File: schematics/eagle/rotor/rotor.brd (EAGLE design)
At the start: 83.8 x 77.5 mm, 55 parts, among them IC1 TXS0108, IC2 7815TV, J1 PL9823, J10 TB004-508-02BE, J2 pwr2, J3 Power, J4 Antenna, J5 Power, J6 CCW, J7 Brake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

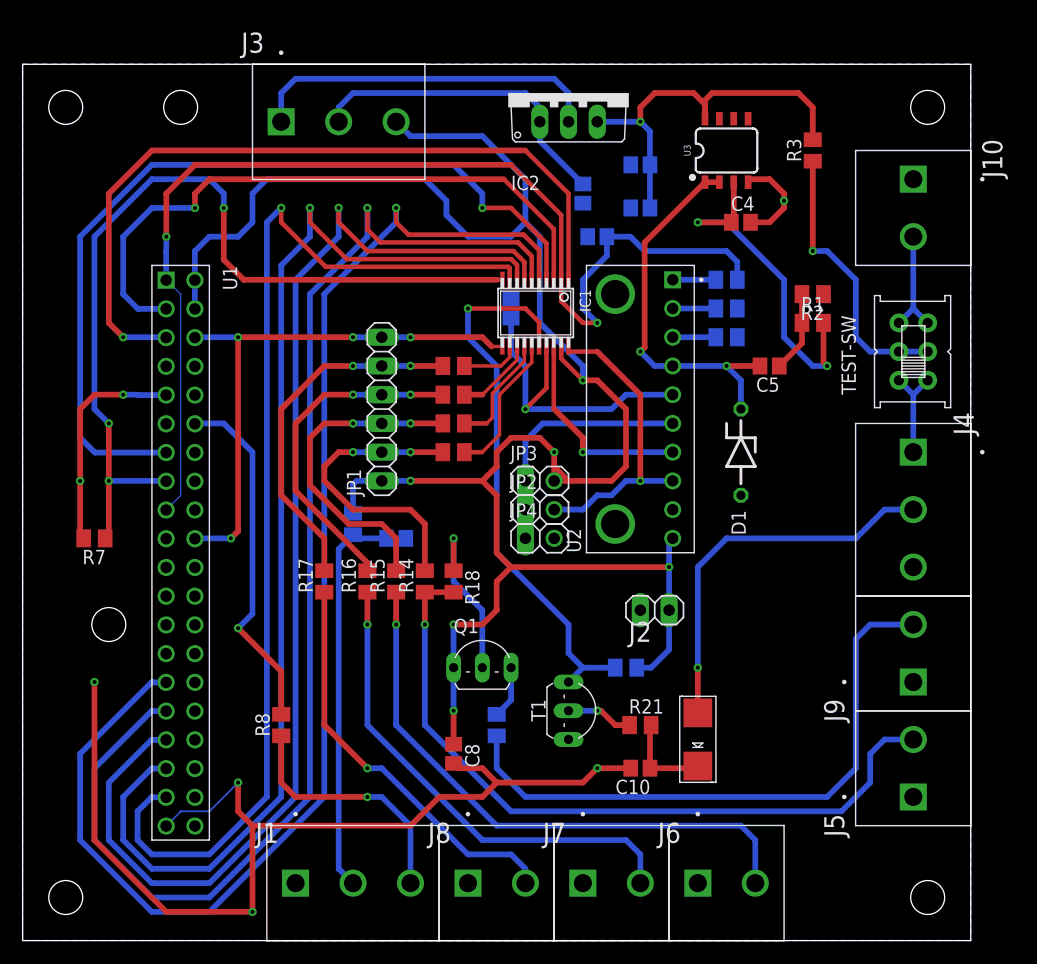
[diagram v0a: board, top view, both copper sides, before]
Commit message: fix rotor input resistor
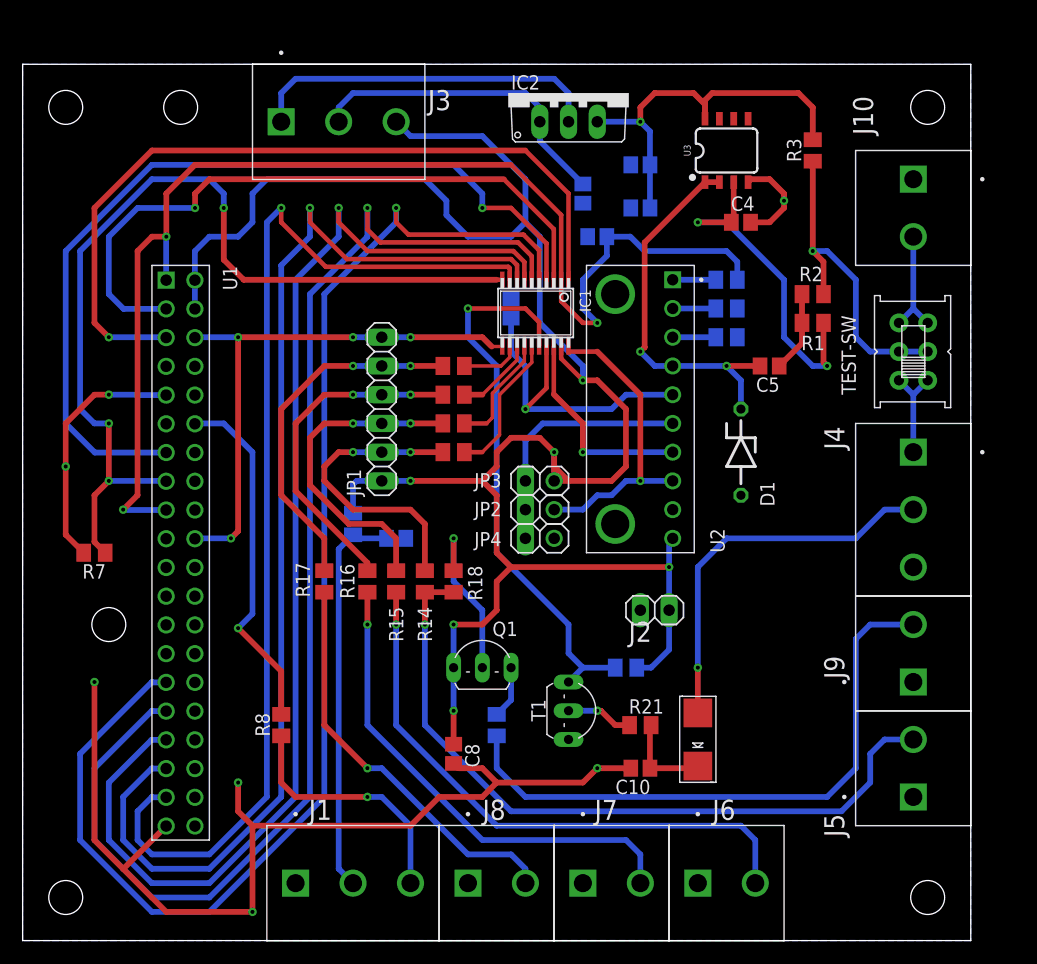
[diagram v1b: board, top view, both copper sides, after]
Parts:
- J10: value TB004-508-02BE -> 500Ω ├
- J9: value Rotor-Pwr-LED -> P.LED
- TEST-SW: value DPDT-SWITCH -> Test-Switch
- moved R7 1.27 mm to (6.35, 34.3)
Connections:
- removed net N$13: R3.1, TEST-SW.C-1, TEST-SW.C-2
- new net INPUT: R2.1, R3.1, TEST-SW.C-1, TEST-SW.C-2
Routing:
- net INPUT: track 0.00 -> 29.0 mm, vias 0 -> 1
- net N$13: track 24.8 -> 0.00 mm, vias 1 -> 0
- net +3.3V: track 101.5 -> 110.4 mm, vias 2 -> 3
- net OE-TXS0108: track 77.7 -> 81.6 mm
- net SDA$1: track 56.7 -> 59.2 mm
- net +5V: track 178.9 -> 181.4 mm
- net SCL$1: track 68.5 -> 70.3 mm
- net ADS1115-ALERT: track 76.6 -> 77.7 mm
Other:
- board text added: "Rotor v1.01"

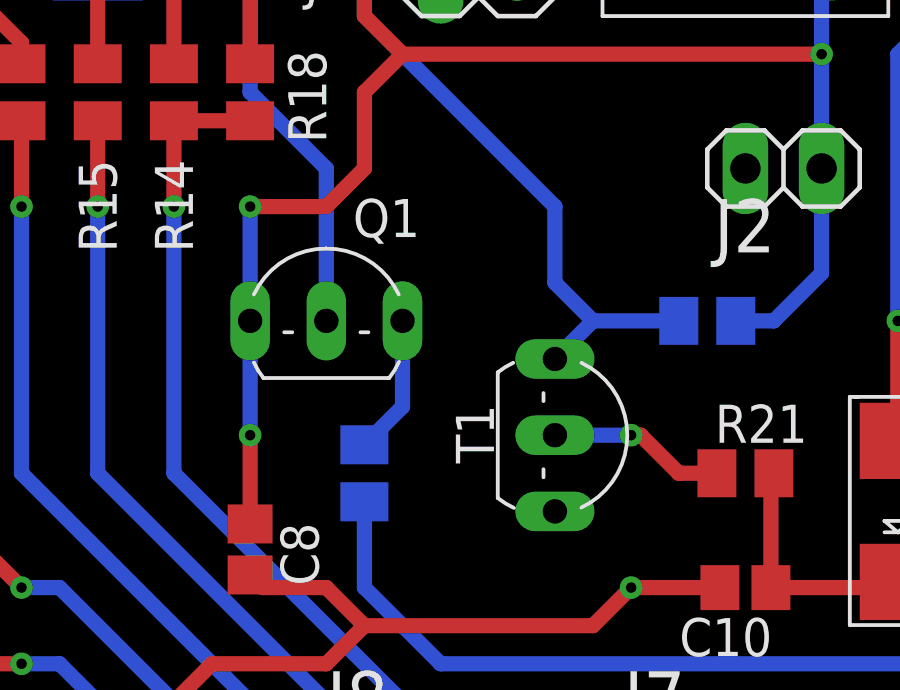
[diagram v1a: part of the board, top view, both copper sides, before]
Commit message: v1.02 - fix transistors
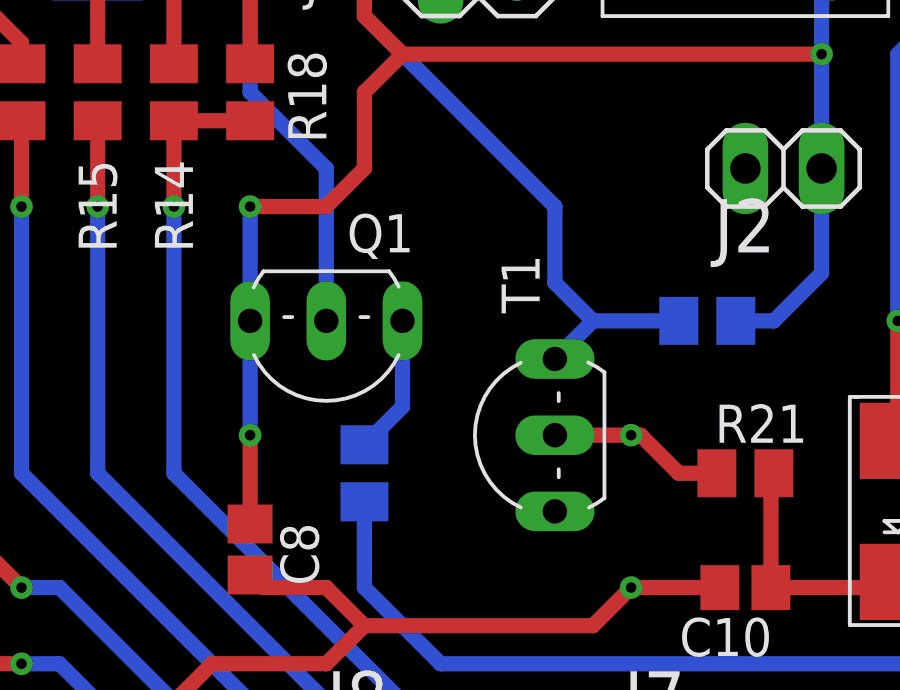
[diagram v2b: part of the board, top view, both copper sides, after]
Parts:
- Q1, T1: device test:TO92-CBE-OVAL -> ladyada:TO92-EBC-OVAL
- moved Q1 2.54 mm to (40.6, 22.9), turned to 180 degrees
- moved T1 2.54 mm to (47.0, 20.3), turned to 90 degrees
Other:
- board text added: "Rotor v1.02"
- board text removed: "Rotor v1.01"
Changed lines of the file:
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@@
 <circle x="13.97" y="73.66" radius="3.175" width="0.1524" layer="105"/>
 <hole x="13.97" y="73.66" drill="3"/>
-<text x="67.31" y="17.78" size="1.778" layer="48" rot="R90">Rotor v1.01</text>
+<text x="67.31" y="17.78" size="1.778" layer="48" rot="R90">Rotor v1.02</text>
 <dimension x1="13.97" y1="78.74" x2="22.86" y2="78.74" x3="18.415" y3="90.17" textsize="1.778" layer="20" dtype="diameter"/>
 <dimension x1="19.05" y1="73.66" x2="19.05" y2="72.39" x3="20.32" y3="73.025" textsize="1.778" layer="20" dtype="diameter"/>
@@
 <attribute name="VALUE" x="39.243" y="32.512" size="1.27" layer="27" rot="R270"/>
 </element>
-<element name="Q1" library="test" package="TO92-CBE-OVAL" value="2N2907" x="40.64" y="25.4" smashed="yes">
-<attribute name="NAME" x="41.529" y="26.924" size="1.27" layer="25" ratio="10"/>
-<attribute name="VALUE" x="30.988" y="23.622" size="1.27" layer="27" ratio="10"/>
+<element name="Q1" library="ladyada" package="TO92-EBC-OVAL" package3d_urn="urn:adsk.eagle:package:6240647/1" value="2N2907" x="40.64" y="22.86" smashed="yes" rot="R180">
+<attribute name="NAME" x="43.561" y="27.686" size="1.27" layer="25" ratio="10" rot="R180"/>
+<attribute name="VALUE" x="36.322" y="24.638" size="1.27" layer="27" ratio="10" rot="R180"/>
 </element>
 <element name="R19" library="test" package="M0805" package3d_urn="urn:adsk.eagle:package:6240587/1" value="1k" x="41.91" y="19.05" smashed="yes" rot="MR90">
@@
 <attribute name="VALUE" x="52.324" y="26.416" size="1.27" layer="28" rot="MR180"/>
 </element>
-<element name="T1" library="test" package="TO92-CBE-OVAL" value="2N2222" x="49.53" y="20.32" smashed="yes" rot="R270">
-<attribute name="NAME" x="44.958" y="21.336" size="1.27" layer="25" ratio="10" rot="R270"/>
-<attribute name="VALUE" x="45.974" y="17.145" size="1.27" layer="27" ratio="10" rot="R90"/>
+<element name="T1" library="ladyada" package="TO92-EBC-OVAL" package3d_urn="urn:adsk.eagle:package:6240647/1" value="2N2222" x="46.99" y="20.32" smashed="yes" rot="R90">
+<attribute name="NAME" x="47.752" y="24.384" size="1.27" layer="25" ratio="10" rot="R90"/>
+<attribute name="VALUE" x="45.466" y="17.145" size="1.27" layer="27" ratio="10" rot="R90"/>
 </element>
 <element name="D2" library="test" package="SMADIODE" package3d_urn="urn:adsk.eagle:package:6240747/1" value="FR107" x="59.69" y="17.78" smashed="yes" rot="R90">
@@
 <wire x1="12.689" y1="10.127" x2="8.912" y2="6.35" width="0.508" layer="1"/>
 <wire x1="8.912" y1="6.35" x2="8.89" y2="6.35" width="0.508" layer="1"/>
+<wire x1="15.229" y1="22.827" x2="15.229" y2="17.747" width="0" layer="19" extent="1-1"/>
+<wire x1="19.05" y1="13.97" x2="15.229" y2="17.747" width="0" layer="19" extent="1-1"/>
 </signal>
 <signal name="+5V">
@@
 <wire x1="53.66" y1="19.05" x2="52.39" y2="19.05" width="0.508" layer="1"/>
 <wire x1="52.39" y1="19.05" x2="51.12" y2="20.32" width="0.508" layer="1"/>
-<wire x1="51.12" y1="20.32" x2="50.8" y2="20.32" width="0.508" layer="1"/>
+<wire x1="51.12" y1="20.32" x2="48.26" y2="20.32" width="0.508" layer="1"/>
 <via x="50.8" y="20.32" extent="1-16" drill="0.35"/>
-<wire x1="50.8" y1="20.32" x2="48.26" y2="20.32" width="0.508" layer="16"/>
+<wire x1="48.26" y1="20.32" x2="50.8" y2="20.32" width="0" layer="19" extent="1-1"/>
 </signal>
 <signal name="ROOF-4">

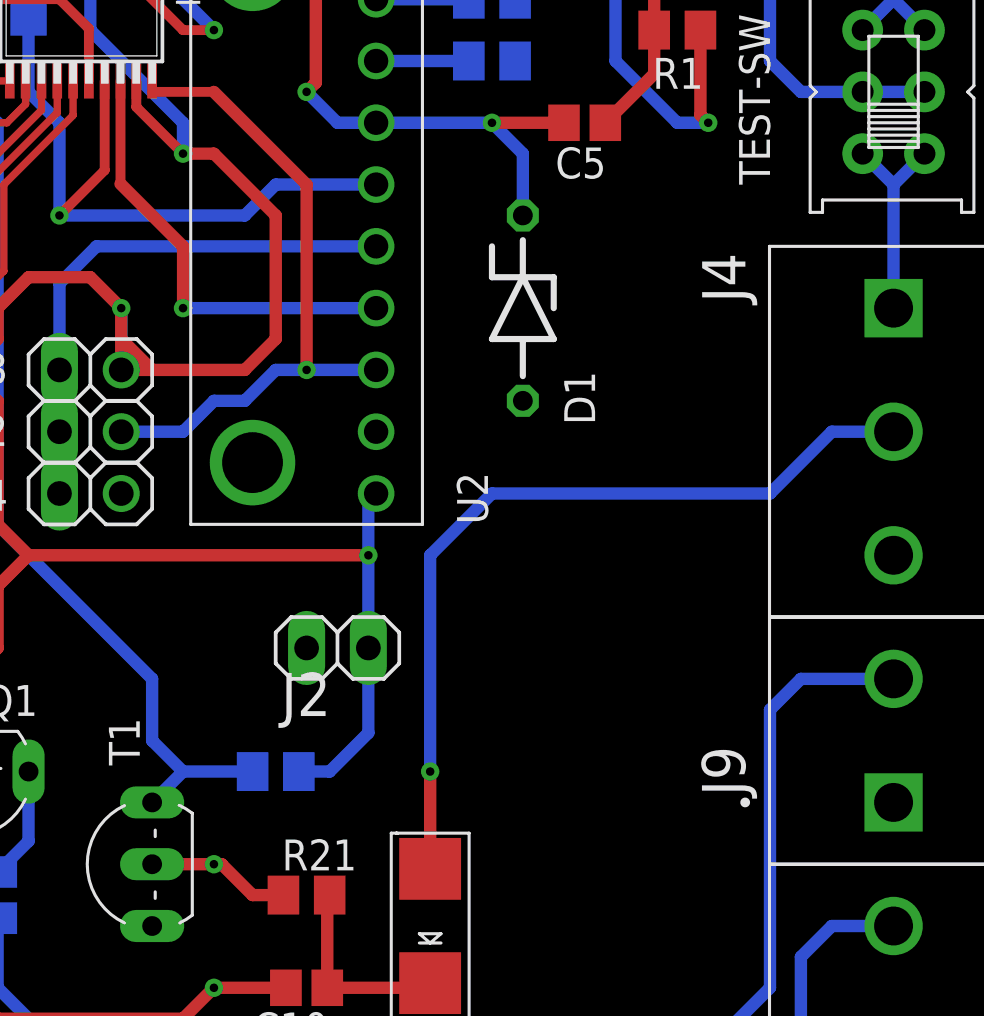
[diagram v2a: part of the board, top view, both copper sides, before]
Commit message: 2n2222 diagram
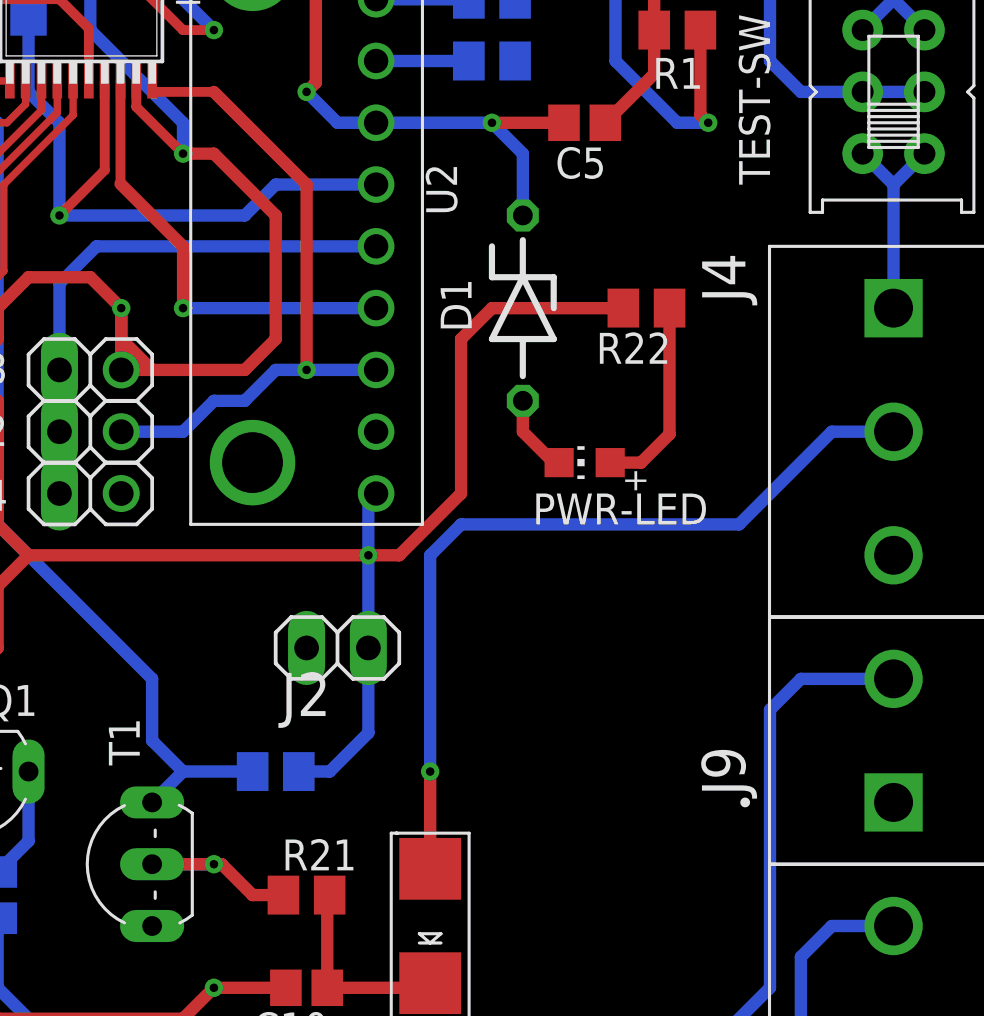
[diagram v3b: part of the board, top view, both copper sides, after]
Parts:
- added PWR-LED: Red, ladyada:CHIP-LED0805
- added R22: 1k, test:M0805
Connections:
- new net N$13: PWR-LED.A, R22.1
- net +5V: now also R22.2
- net GND: now also PWR-LED.C
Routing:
- net +5V: track 181.4 -> 199.8 mm
- net N$13: track 0.00 -> 8.10 mm
- net GND: track 198.9 -> 202.1 mm
- net N$12: track 5.93 -> 8.47 mm
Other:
- board text added: "Rotor v1.03"
- board text removed: "Rotor v1.02"
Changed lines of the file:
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@@
 <circle x="13.97" y="73.66" radius="3.175" width="0.1524" layer="105"/>
 <hole x="13.97" y="73.66" drill="3"/>
-<text x="67.31" y="17.78" size="1.778" layer="48" rot="R90">Rotor v1.02</text>
+<text x="67.31" y="17.78" size="1.778" layer="48" rot="R90">Rotor v1.03</text>
 <dimension x1="13.97" y1="78.74" x2="22.86" y2="78.74" x3="18.415" y3="90.17" textsize="1.778" layer="20" dtype="diameter"/>
-<dimension x1="19.05" y1="73.66" x2="19.05" y2="72.39" x3="20.32" y3="73.025" textsize="1.778" layer="20" dtype="diameter"/>
-<dimension x1="17.78" y1="27.94" x2="17.78" y2="5.08" x3="20.32" y3="16.51" textsize="1.778" layer="20" dtype="diameter"/>
 <dimension x1="24.13" y1="3.81" x2="7.62" y2="3.81" x3="15.875" y3="-8.89" textsize="1.778" layer="20" dtype="diameter"/>
 </plain>
@@
 <attribute name="MF" value="Adafruit Industries" x="50.8" y="46.99" size="1.778" layer="27" rot="R90" display="off"/>
 <attribute name="MP" value="1085" x="50.8" y="46.99" size="1.778" layer="27" rot="R90" display="off"/>
-<attribute name="NAME" x="62.0655" y="34.29" size="1.27" layer="25" rot="R90"/>
+<attribute name="NAME" x="60.7955" y="46.99" size="1.27" layer="25" rot="R90"/>
 <attribute name="PACKAGE" value="None" x="50.8" y="46.99" size="1.778" layer="27" rot="R90" display="off"/>
 <attribute name="PRICE" value="None" x="50.8" y="46.99" size="1.778" layer="27" rot="R90" display="off"/>
@@
 </element>
 <element name="D1" library="diode" library_urn="urn:adsk.eagle:library:210" package="ZDIO-7.5" package3d_urn="urn:adsk.eagle:package:43411/1" value="5.1v 2%" x="63.5" y="43.18" smashed="yes" rot="R270">
-<attribute name="NAME" x="65.2018" y="40.5892" size="1.27" layer="25" ratio="10" rot="R270"/>
+<attribute name="NAME" x="60.1218" y="44.3992" size="1.27" layer="25" ratio="10" rot="R270"/>
 <attribute name="POPULARITY" value="6" x="63.5" y="43.18" size="1.778" layer="27" rot="R270" display="off"/>
 <attribute name="VALUE" x="65.532" y="45.72" size="1.27" layer="27" ratio="10" rot="R270"/>
@@
 <attribute name="PURCHASE-URL" value="https://pricing.snapeda.com/search/part/TB004-508-02BE/?ref=eda" x="78.74" y="67.31" size="1.778" layer="27" rot="R270" display="off"/>
 <attribute name="VALUE" x="71.39" y="68.31" size="1.778" layer="27" rot="R270"/>
+</element>
+<element name="R22" library="test" package="M0805" package3d_urn="urn:adsk.eagle:package:6240587/1" value="1k" x="68.58" y="43.18" smashed="yes" rot="R180">
+<attribute name="NAME" x="69.596" y="42.164" size="1.27" layer="25" rot="R180"/>
+<attribute name="VALUE" x="69.596" y="45.466" size="1.27" layer="27" rot="R180"/>
+</element>
+<element name="PWR-LED" library="ladyada" package="CHIP-LED0805" package3d_urn="urn:adsk.eagle:package:6240557/1" value="Red" x="66.04" y="36.83" smashed="yes" rot="R90">
+<attribute name="NAME" x="71.12" y="35.56" size="1.27" layer="25" rot="R180"/>
+<attribute name="VALUE" x="67.31" y="39.37" size="1.27" layer="27" rot="R180"/>
 </element>
 </elements>
@@
 <wire x1="12.689" y1="10.127" x2="8.912" y2="6.35" width="0.508" layer="1"/>
 <wire x1="8.912" y1="6.35" x2="8.89" y2="6.35" width="0.508" layer="1"/>
-<wire x1="15.229" y1="22.827" x2="15.229" y2="17.747" width="0" layer="19" extent="1-1"/>
-<wire x1="19.05" y1="13.97" x2="15.229" y2="17.747" width="0" layer="19" extent="1-1"/>
+<contactref element="PWR-LED" pad="C"/>
+<wire x1="64.99" y1="36.83" x2="64.77" y2="36.83" width="0.508" layer="1"/>
+<wire x1="64.77" y1="36.83" x2="63.5" y2="38.1" width="0.508" layer="1"/>
+<wire x1="63.5" y1="38.1" x2="63.5" y2="39.37" width="0.508" layer="1"/>
 </signal>
 <signal name="+5V">
@@
 <wire x1="38.1" y1="24.13" x2="38.1" y2="20.32" width="0.508" layer="16"/>
 <wire x1="46.99" y1="43.18" x2="46.99" y2="40.64" width="0.508" layer="16"/>
+<contactref element="R22" pad="2"/>
+<wire x1="67.63" y1="43.18" x2="62.23" y2="43.18" width="0.508" layer="1"/>
+<wire x1="60.96" y1="41.91" x2="60.96" y2="35.56" width="0.508" layer="1"/>
+<wire x1="57.15" y1="33.02" x2="58.42" y2="33.02" width="0.508" layer="1"/>
+<wire x1="60.96" y1="35.56" x2="58.42" y2="33.02" width="0.508" layer="1"/>
+<wire x1="62.23" y1="43.18" x2="60.96" y2="41.91" width="0.508" layer="1"/>
 </signal>
 <signal name="ADDR">
@@
 <wire x1="51.12" y1="20.32" x2="48.26" y2="20.32" width="0.508" layer="1"/>
 <via x="50.8" y="20.32" extent="1-16" drill="0.35"/>
-<wire x1="48.26" y1="20.32" x2="50.8" y2="20.32" width="0" layer="19" extent="1-1"/>
+<wire x1="50.8" y1="20.32" x2="48.26" y2="20.32" width="0.508" layer="16"/>
 </signal>
 <signal name="ROOF-4">
@@
 <wire x1="59.69" y1="33.02" x2="59.69" y2="24.13" width="0.508" layer="16"/>
 <wire x1="78.74" y1="38.1" x2="76.2" y2="38.1" width="0.508" layer="16"/>
-<wire x1="73.66" y1="35.56" x2="62.23" y2="35.56" width="0.508" layer="16"/>
-<wire x1="62.23" y1="35.56" x2="59.69" y2="33.02" width="0.508" layer="16"/>
-<wire x1="76.2" y1="38.1" x2="73.66" y2="35.56" width="0.508" layer="16"/>
+<wire x1="72.39" y1="34.29" x2="60.96" y2="34.29" width="0.508" layer="16"/>
+<wire x1="60.96" y1="34.29" x2="59.69" y2="33.02" width="0.508" layer="16"/>
+<wire x1="76.2" y1="38.1" x2="72.39" y2="34.29" width="0.508" layer="16"/>
 </signal>
 <signal name="N$9">
@@
 <wire x1="78.74" y1="62.23" x2="78.74" y2="55.88" width="0.508" layer="16"/>
 </signal>
+<signal name="N$13">
+<contactref element="PWR-LED" pad="A"/>
+<contactref element="R22" pad="1"/>
+<wire x1="69.53" y1="43.18" x2="69.53" y2="38" width="0.508" layer="1"/>
+<wire x1="69.53" y1="38" x2="68.36" y2="36.83" width="0.508" layer="1"/>
+<wire x1="67.09" y1="36.83" x2="68.36" y2="36.83" width="0.508" layer="1"/>
+</signal>
 </signals>
